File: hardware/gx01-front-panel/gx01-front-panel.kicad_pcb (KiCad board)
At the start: 2 copper layers, 65 x 30 mm, 24 parts, among them J1 Cable, SW1 UP, SW2 DOWN, SW3 LEFT, SW4 RIGHT, SW5 SELECT, SW6 BACK, U1 MCP23017, U2 VEML7700

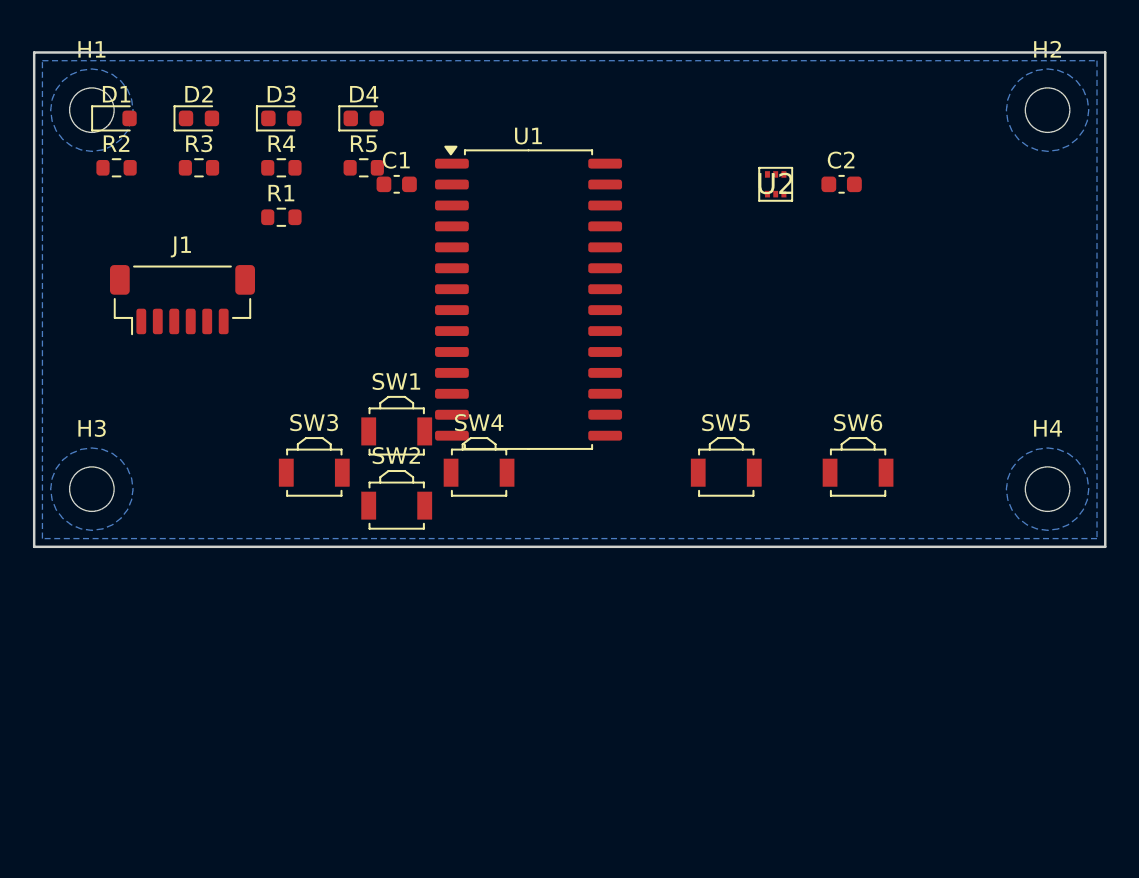
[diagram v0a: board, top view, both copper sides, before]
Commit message: feat(hardware): GX-01 Front Panel Board — full pipeline through JLC bundle
Same scripted pipeline as the main HAT, now applied to the FPB:
  circuit.py (existing, ERC-clean)
  → layout.py (reworked: 65×30 → 65×42 mm, proper D-pad layout)
  → autoroute.py (converged, 217 tracks, 0 unconnected)
  → kicad-cli DRC (6 warnings, all cosmetic silk/library)
  → kicad-cli gerbers + drill
  → make_jlc_bundle.py → jlc_bundle.zip

Board expanded from 65×30 mm → 65×42 mm after first render showed
MCP23017 SOIC-28W (17.9 mm long) leaving no clean space for the 6
tactile switches below it.

Placement:
  Top strip (Y≈6-9): D1-D4 LEDs + R2-R5 current-limits on 5 mm pitch
  Mid strip (Y≈10-17): MCP23017, J1 JST-SH cable, bypass caps, reset pull-up
  Bottom strip (Y≈22-34): 6 tactile switches in D-pad + Select + Back
  Upper right: VEML7700 ambient light sensor near case window

All LCSC codes verified in-stock on 2026-04-19 via JLC's PCBA search API:
  J1 C160392  JST BM06B-SRSS-TB    9,211
  U1 C629440  MCP23017T-E/SO       1,816
  U2 C504893  VEML7700-TR          2,003  (JLC spec says SMD-4P; actual
                                         OPLGA-6 has 6 pads — watch the
                                         3D preview for mismatch)
  SW C963349  Omron B3U-3000P      3,910
  D1 C12624   0603 Green           212k
  D2 C2288    0603 Blue            207k
  D3 C2287    0603 Yellow          15k
  D4 C2286    0603 Red             7.2M
  R1 C25804   10k 0603             Basic
  R2-R5 C21190 1k 0603             Basic  (25M+ in stock)
  C1-C2 C14663 100nF 0603          Basic

Bundle: 24 components, 4 skipped (H1-H4), 20 assembled (11 Basic + 9
Extended), ~$27 feeder fees.

One residual DRC warning worth flagging: the custom
geographica:VEML7700_OPLGA-6 footprint has the reference text
overlapping its own 2×2 mm body outline. Cosmetic.

Co-Authored-By: Claude Opus 4.7 (1M context) <noreply@anthropic.com>
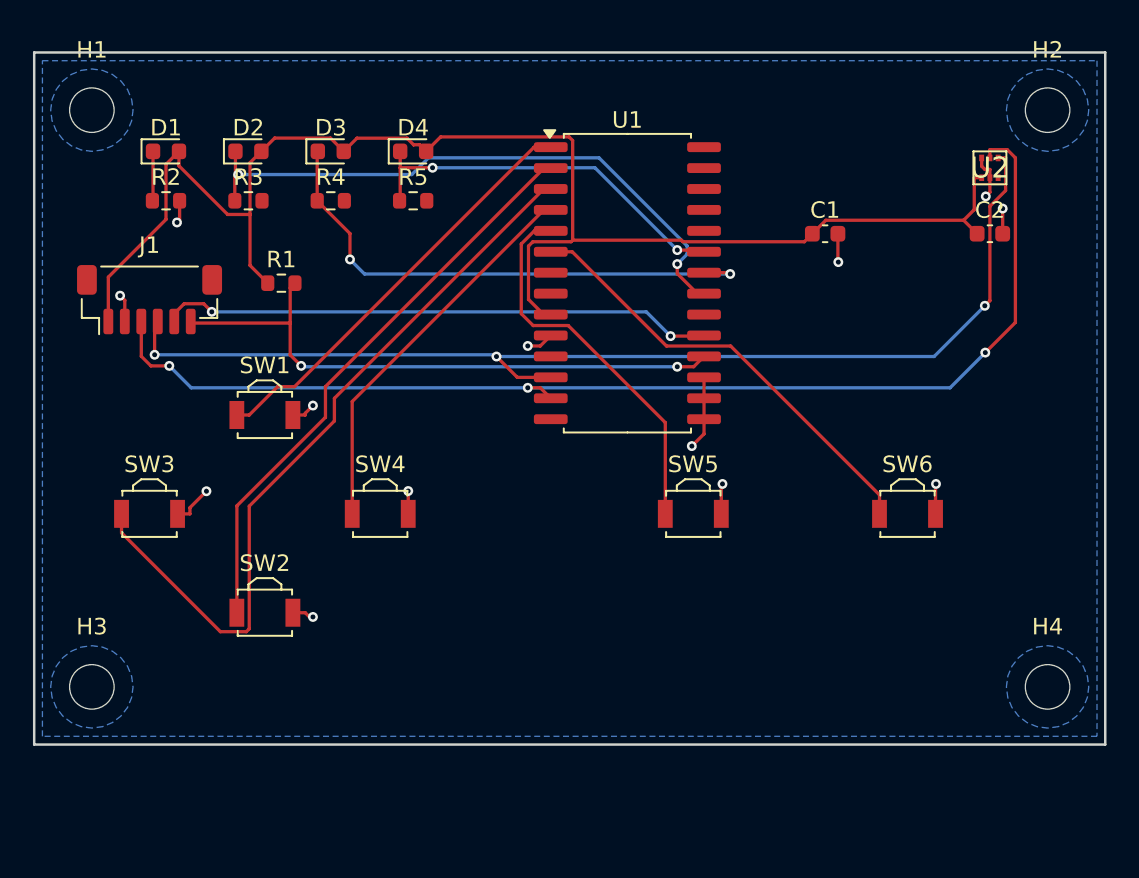
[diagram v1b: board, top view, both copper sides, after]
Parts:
- D1: value PWR -> PWR_Grn
- D2: value GPS -> GPS_Blu
- D3: value NTP -> NTP_Yel
- D4: value ERR -> ERR_Red
- moved C1 26.2 mm to (48.0, 11.0)
- moved U2 13.0 mm to (58.0, 7.00)
- moved H3 12.0 mm to (3.50, 38.5)
- moved H4 12.0 mm to (61.5, 38.5)
- moved SW2 10.3 mm to (14.0, 34.0)
- moved SW3 10.3 mm to (7.00, 28.0)
- moved C2 9.49 mm to (58.0, 11.0)
- moved SW1 8.06 mm to (14.0, 22.0)
- moved SW4 6.50 mm to (21.0, 28.0)
- moved U1 6.08 mm to (36.0, 14.0)
- moved R1 4.00 mm to (15.0, 14.0)
- moved SW6 3.91 mm to (53.0, 28.0)
- moved D1 3.61 mm to (8.00, 6.00)
- moved D2 3.61 mm to (13.0, 6.00)
- moved D3 3.61 mm to (18.0, 6.00)
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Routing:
- net +3V3: track 0.00 -> 90.5 mm
- net SDA1: track 0.00 -> 71.5 mm, vias 0 -> 3
- net SCL1: track 0.00 -> 67.6 mm, vias 0 -> 3
- net SW_LEFT: track 0.00 -> 46.0 mm
- net D2_K: track 0.00 -> 37.1 mm, vias 0 -> 2
- net MCP_RST: track 0.00 -> 36.2 mm, vias 0 -> 2
- net SW_DOWN: track 0.00 -> 35.1 mm
- net MCP_INT: track 0.00 -> 33.7 mm, vias 0 -> 2
- net D3_K: track 0.00 -> 32.6 mm, vias 0 -> 2
- net SW_BACK: track 0.00 -> 27.2 mm
- net SW_UP: track 0.00 -> 25.8 mm
- net GND: track 0.00 -> 25.7 mm, vias 0 -> 13
- net SW_RIGHT: track 0.00 -> 23.7 mm
- net D4_K: track 0.00 -> 23.6 mm, vias 0 -> 2
- net SW_SEL: track 0.00 -> 23.4 mm
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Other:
- board size 65 x 30 mm -> 65 x 42 mm

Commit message: fix(hardware): swap FPB switches from B3U (side-actuated) to B3S (top-actuated)
Cameron caught in the JLC preview that all 6 FPB switches had their
actuators pointing toward the top of the board (XY direction) instead
of out from the board (Z axis toward the user). The B3U series is
designed for side-actuation — pressed parallel to the PCB, e.g. through
a case's side wall — which is unusable for a case front panel where the
user presses buttons perpendicular to the board surface.

Swapped to Omron B3S-1000P — top-actuated 6×6×5 mm SMD tactile with 4
pads at corners (±4×±2.25 mm). Both pad pairs are internally shorted;
duplicate pad numbers (two "1"s for signal, two "2"s for GND) require
setting the net on EVERY pad matching a given number, not just the
first one FindPadByNumber returns.

Changes:
  circuit.py: footprint Button_Switch_SMD:SW_SPST_B3S-1000
  layout.py:
    - connect() now iterates all pads matching pad_num (was: first only)
    - Board grew 42 mm → 48 mm tall to accommodate 6×6 body + proper
      D-pad spacing + mounting-hole keepouts
    - D-pad layout: SW1 above row, SW3/SW4 flanking, SW2 below row
    - SW5/SW6 as separate buttons on the right
  lcsc_mapping.yaml: SW1-SW6 C963349 → C180420 (Omron B3S-1000P, 4,770
    in stock verified 2026-04-19)
  layout_v2b.py (main HAT): same connect_pad fix for CR1632 holder
    which also uses duplicate pad numbers for its two anode/cathode
    contacts. Without this fix, half the physical supercap/coin-cell
    pads were unnetted and unrouted.

Rotation correction still picks up the ^SW_SPST_B3 DB entry at +90°,
which matches both B3U and B3S families. FPB autoroute reconverged
cleanly: 245 tracks, 0 unconnected pads.

Co-Authored-By: Claude Opus 4.7 (1M context) <noreply@anthropic.com>
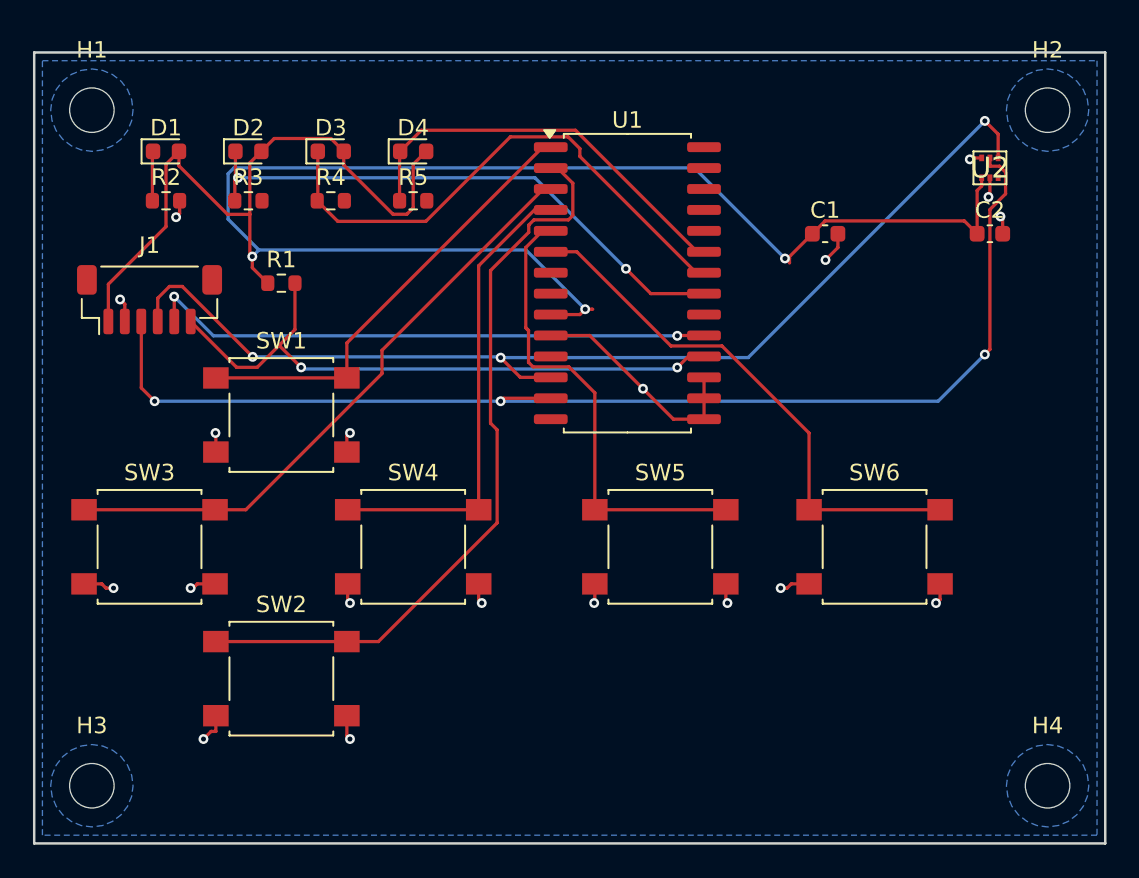
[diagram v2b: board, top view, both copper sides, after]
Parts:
- SW1, SW2, SW3, SW4, SW5, SW6: footprint SW_SPST_B3U-3000P -> SW_SPST_B3S-1000
- moved H3 6.00 mm to (3.50, 44.5)
- moved H4 6.00 mm to (61.5, 44.5)
- moved SW2 4.12 mm to (15.0, 38.0)
- moved SW4 2.83 mm to (23.0, 30.0)
- moved SW5 2.83 mm to (38.0, 30.0)
- moved SW6 2.83 mm to (51.0, 30.0)
- moved SW3 2.00 mm to (7.00, 30.0)
- moved SW1 1.00 mm to (15.0, 22.0)
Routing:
- net +3V3: track 90.5 -> 126.1 mm, vias 0 -> 3
- net GND: track 25.7 -> 38.7 mm, vias 13 -> 19
- net SW_DOWN: track 35.1 -> 45.8 mm
- net SW_LEFT: track 46.0 -> 37.2 mm
- net SW_SEL: track 23.4 -> 29.0 mm
- net SW_BACK: track 27.2 -> 32.8 mm
- net SW_RIGHT: track 23.7 -> 28.5 mm
- net D2_K: track 37.1 -> 34.4 mm
- net SCL1: track 67.6 -> 65.8 mm
- net MCP_RST: track 36.2 -> 37.9 mm
- net SW_UP: track 25.8 -> 27.4 mm
- net SDA1: track 71.5 -> 73.0 mm
- net D4_K: track 23.6 -> 25.0 mm, vias 2 -> 0
- net MCP_INT: track 33.7 -> 34.7 mm
- net D3_K: track 32.6 -> 32.8 mm, vias 2 -> 0
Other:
- board size 65 x 42 mm -> 65 x 48 mm
